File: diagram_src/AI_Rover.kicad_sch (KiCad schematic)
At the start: 13 parts, among them J1 GPIO_PINS, J2 LOGIC_PINS, J3 LOGIC_PINS, J5 POWER_PINS, J6 POWER_PINS, M1 MOTOR_DC_LEFT, M2 MOTOR_DC_RIGHT, SW1 MAIN_POWER_SWITCH

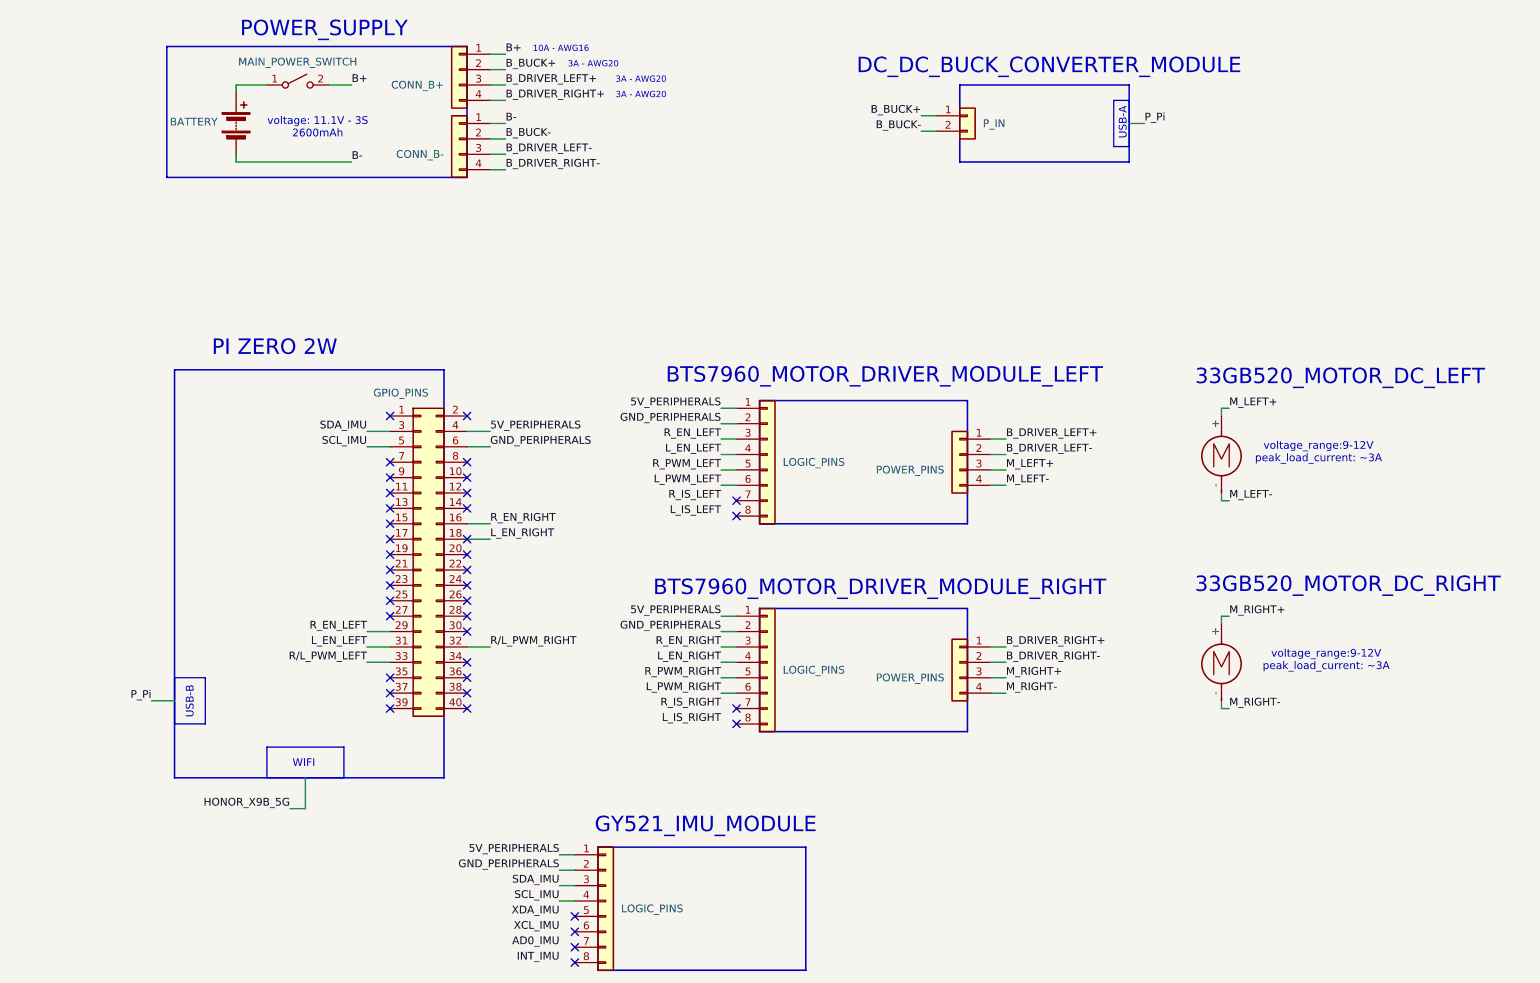
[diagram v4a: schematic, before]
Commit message: Hardware: Finallize wiring schematic
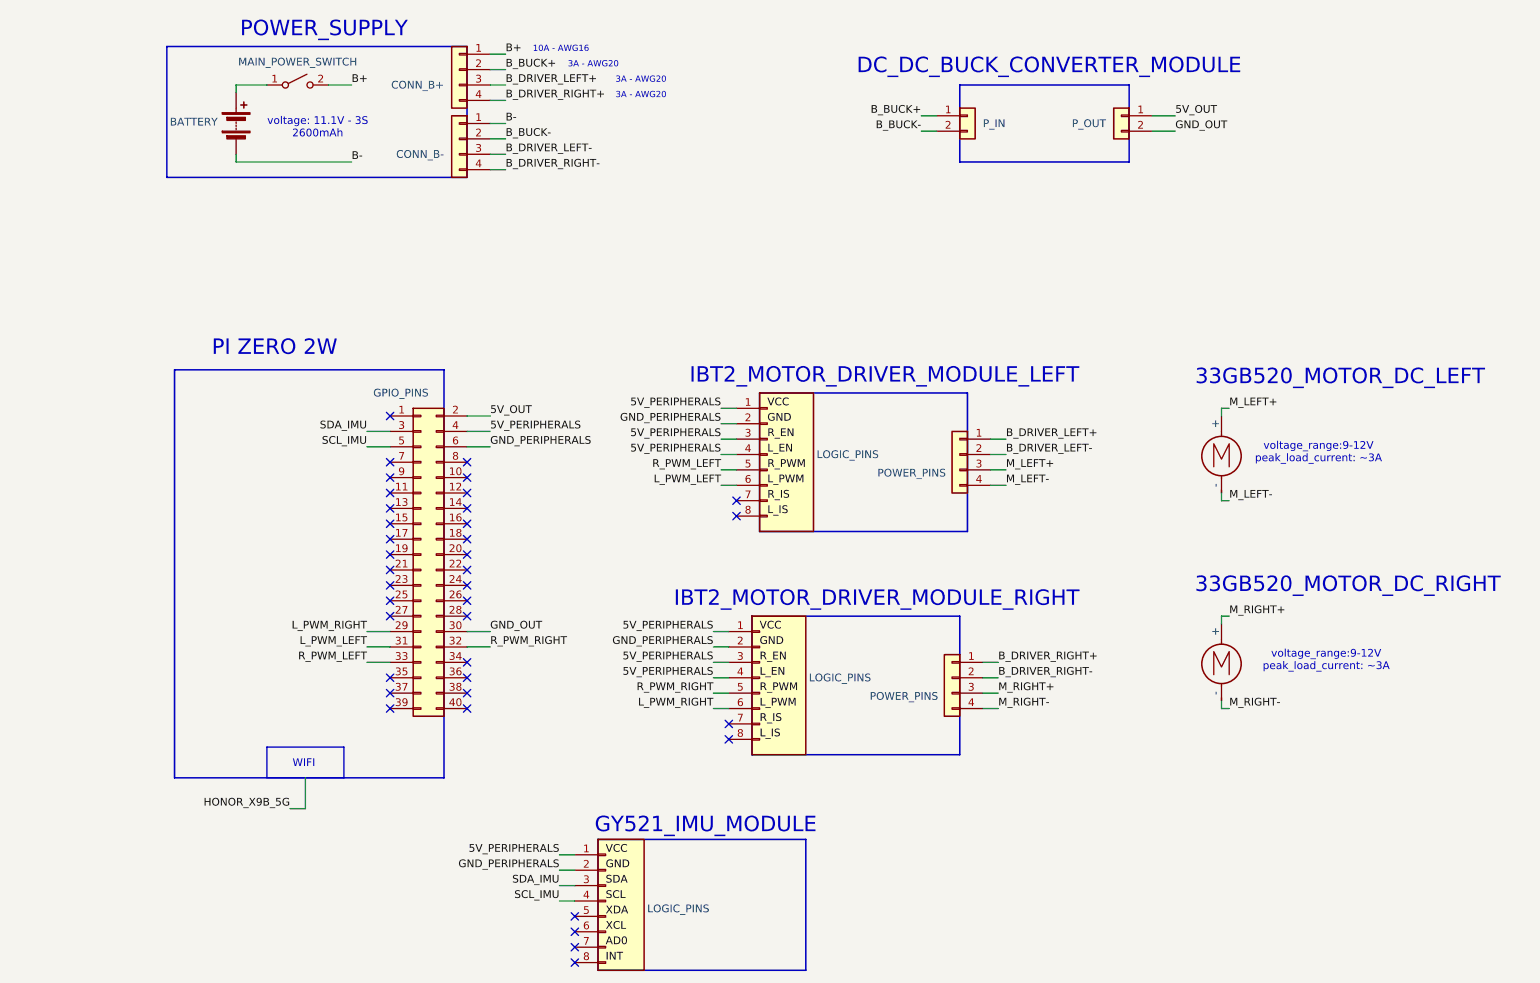
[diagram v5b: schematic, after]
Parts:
- added J4: P_OUT, symbol Connector_Generic:Conn_01x02
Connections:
- net R/L_PWM_LEFT is gone; now on net R_PWM_LEFT: J1.33 (Pin_33)
- net R/L_PWM_RIGHT is gone; now on net R_PWM_RIGHT: J1.32 (Pin_32)
- net 5V_PERIPHERALS: now also J2.3 (Pin_3), J2.4 (Pin_4), J3.3 (Pin_3), J3.4 (Pin_4)
- net L_PWM_LEFT: now also J1.31 (Pin_31)
- net L_PWM_RIGHT: now also J1.29 (Pin_29)
- net 5V_OUT: now reaches J1.2 (Pin_2)
- net 5V_OUT: now also J4.1 (Pin_1)
- net GND_OUT: now reaches J1.30 (Pin_30)
- net GND_OUT: now also J4.2 (Pin_2)
- removed net L_EN_LEFT: J1.31 (Pin_31), J2.4 (Pin_4)
- net L_EN_RIGHT: no longer names the net of J1.18 (Pin_18)
- net L_EN_RIGHT: no longer J3.4 (Pin_4)
- removed net R_EN_LEFT: J1.29 (Pin_29), J2.3 (Pin_3)
- net R_EN_RIGHT: no longer names the net of J1.16 (Pin_16)
- net R_EN_RIGHT: no longer J3.3 (Pin_3)
- no-connect marks 39 -> 38
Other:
- note added: "IBT2_MOTOR_DRIVER_MODULE_LEFT"
- note added: "IBT2_MOTOR_DRIVER_MODULE_RIGHT"
- note removed: "BTS7960_MOTOR_DRIVER_MODULE_LEFT"
- note removed: "BTS7960_MOTOR_DRIVER_MODULE_RIGHT"
- note removed: "USB-A"
- note removed: "USB-B"
